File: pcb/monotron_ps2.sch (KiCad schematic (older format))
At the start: 7 parts, among them J13 DB25_Female, J14 Mini-DIN-6, J15 Mini-DIN-6, U5 ATmega48A-PU

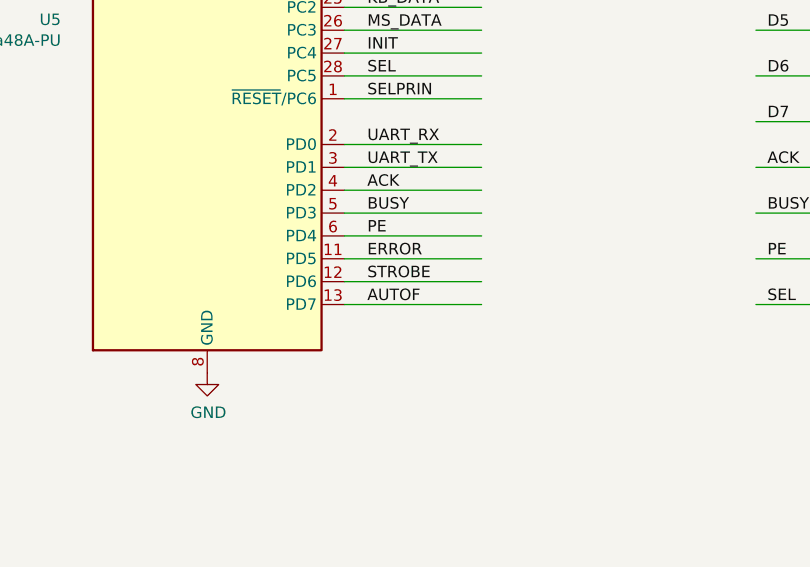
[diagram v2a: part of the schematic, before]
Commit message: Finished adding RTC to PCB layout.
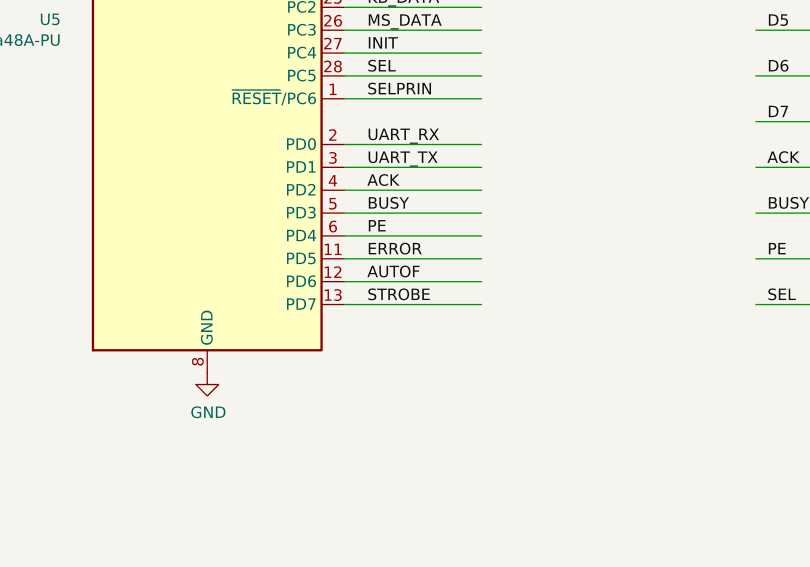
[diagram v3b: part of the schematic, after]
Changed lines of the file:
@@
 ERROR
 Text Label 4600 4150 0    50   ~ 0
+AUTOF
+Text Label 4600 4250 0    50   ~ 0
 STROBE
-Text Label 4600 4250 0    50   ~ 0
-AUTOF
 Text Label 4600 3150 0    50   ~ 0
 INIT

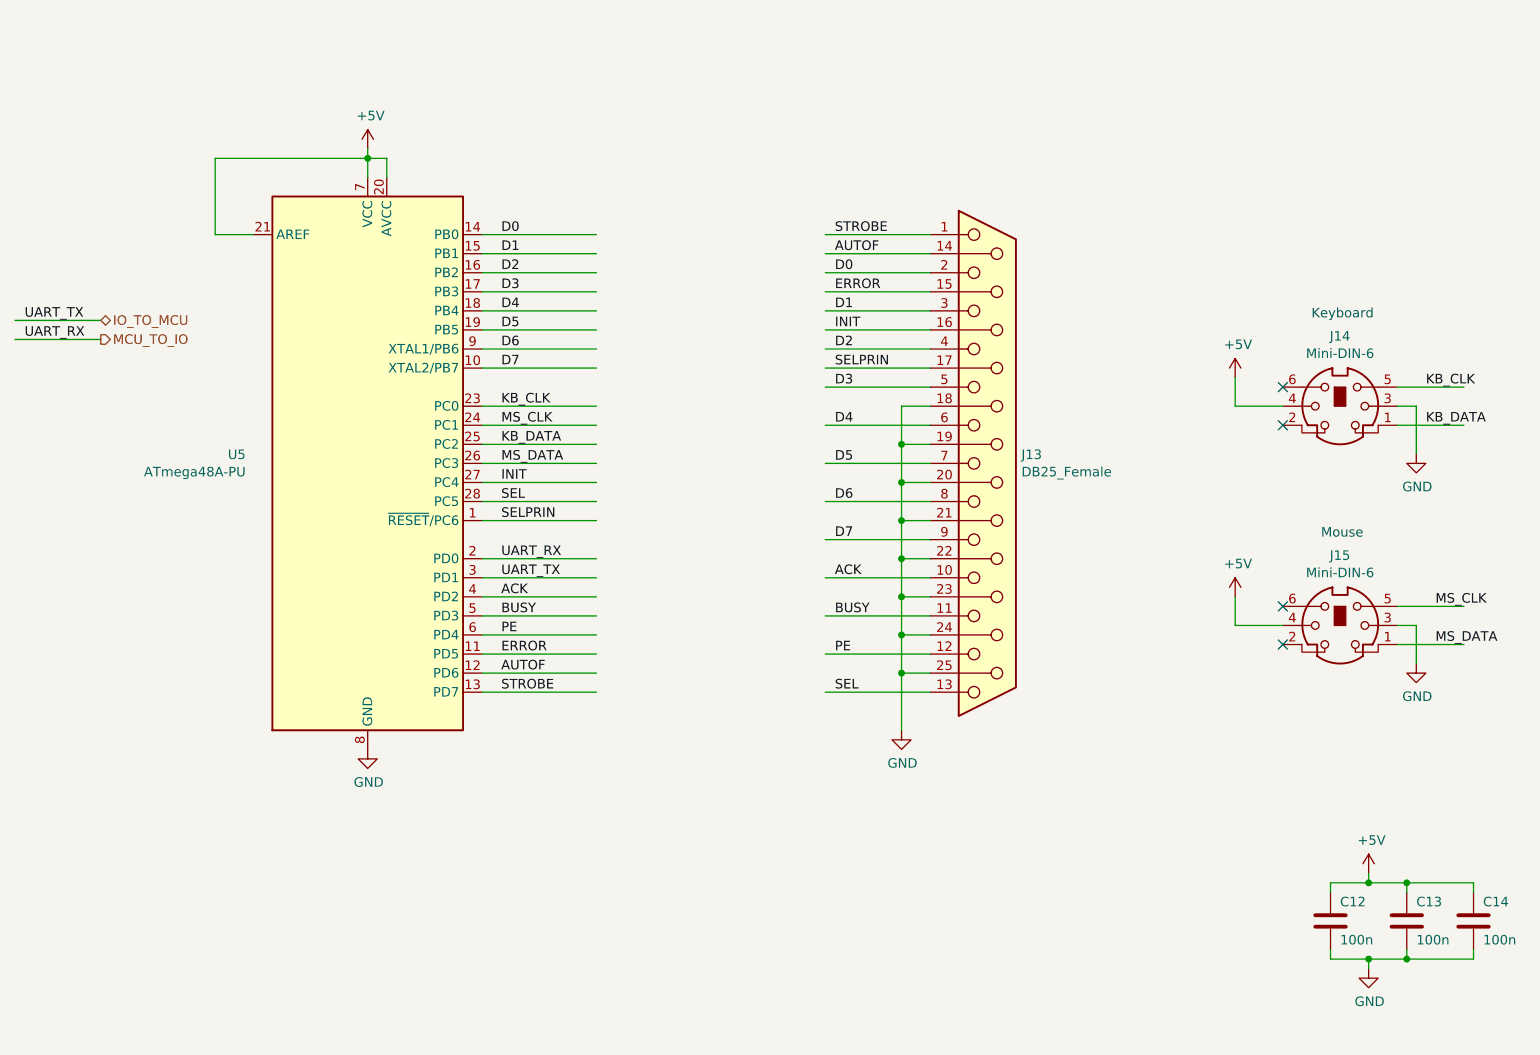
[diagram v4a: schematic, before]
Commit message: Updated Schematic to 0.8.0. (PCB layout still at 0.7.0). Added BOM.
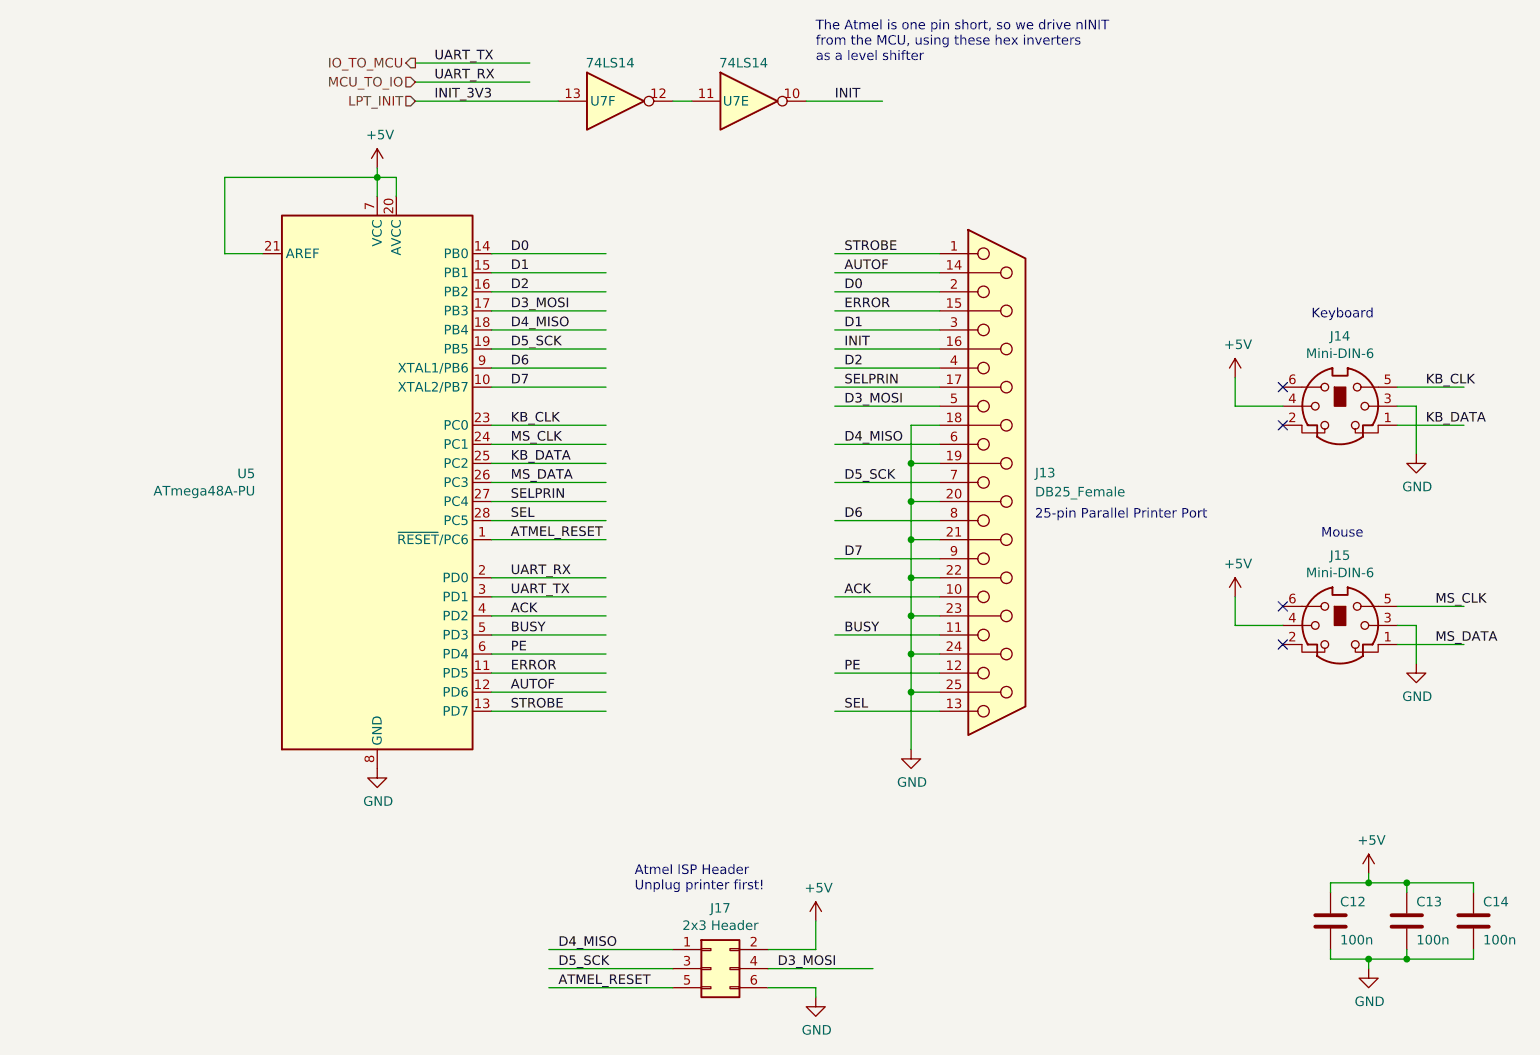
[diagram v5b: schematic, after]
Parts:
- added J17: 2x3 Header, symbol Connector_Generic:Conn_02x03_Odd_Even
- added U7: 74LS14, Package_DIP:DIP-14_W7.62mm, symbol 74xx:74LS14
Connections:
- net labels added: ATMEL_RESET, D3_MOSI, D4_MISO, D5_SCK, INIT_3V3, LPT_INIT
- net labels removed: D3, D4, D5
- wire segments 91 -> 102
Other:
- note added: "25-pin Parallel Printer Port"
- note added: "Atmel ISP Header\nUnplug printer first!"
- note added: "The Atmel is one pin short, so we drive nINIT\nfrom the MCU, using these hex inverters\nas a level shifter"
- moved on the sheet: J13, U5
